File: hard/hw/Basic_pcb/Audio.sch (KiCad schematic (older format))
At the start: 0 parts

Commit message: Bloque de Audio
Bloque de Audio implementado PAM8302 de adafruit:
https://www.adafruit.com/product/2130
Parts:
- added C1: 10uF, Capacitors_SMD:C_0805, symbol C
- added C2, C3: 1uF, Capacitors_SMD:C_0805, symbol C
- added C4, C5: 220pF, Capacitors_SMD:C_0805, symbol C
- added L1, L2: Ferrite_Bead, Resistors_SMD:R_0805, symbol Ferrite_Bead
- added P1: CONN_01X05, Socket_Strips:Socket_Strip_Straight_1x05_Pitch2.54mm, symbol CONN_01X05
- added P2: CONN_01X02, Socket_Strips:Socket_Strip_Straight_1x02_Pitch2.54mm, symbol CONN_01X02
- added R1: 10K, Resistors_SMD:R_0805, symbol R
- added R2, R3: 100, Resistors_SMD:R_0805, symbol R
- added RV1: 10K POT_TRIM, Potentiometers:Potentiometer_Trimmer-EVM3E, symbol POT_TRIM
- added U1: PAM8302A, Housings_SSOP:MSOP-8_3x3mm_Pitch0.65mm, symbol PAM8302A
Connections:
- net labels added: +5V, AIN+, AIN-, GND, ~SD
- wire segments 0 -> 36

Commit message: Actualizacion Power
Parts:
- removed P1: CONN_01X05, Socket_Strips:Socket_Strip_Straight_1x05_Pitch2.54mm, symbol CONN_01X05
- added P?: CONN_01X05, symbol CONN_01X05
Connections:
- net labels added: VCC
- wire segments 36 -> 39
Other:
- moved on the sheet: C1, R1
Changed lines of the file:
@@
 LIBS:rj45_stamp
 LIBS:HDMIspartan6_Board-cache
-LIBS:pam8302-cache
 EELAYER 25 0
 EELAYER END
 $Descr A4 11693 8268
 encoding utf-8
-Sheet 4 5
+Sheet 3 5
 Title ""
 Date ""
@@
 L C C1
 U 1 1 5898CF7F
-P 4650 5400
-F 0 "C1" H 4500 5500 50  0000 L CNN
-F 1 "10uF" H 4450 5300 50  0000 L CNN
-F 2 "Capacitors_SMD:C_0805" H 5200 5400 50  0001 C CNN
-F 3 "" H 4650 5400 50  0000 C CNN
-	1    4650 5400
-	-1   0    0    1
+P 3050 5100
+F 0 "C1" H 2950 5200 50  0000 L CNN
+F 1 "10uF" H 2850 5000 50  0000 L CNN
+F 2 "Capacitors_SMD:C_0805" H 3600 5100 50  0001 C CNN
+F 3 "" H 3050 5100 50  0000 C CNN
+	1    3050 5100
+	-1   0    0    -1
 $EndComp
 $Comp
 L R R1
 U 1 1 5898CF80
-P 5050 5200
-F 0 "R1" V 5130 5200 50  0000 C CNN
-F 1 "10K" V 5050 5200 50  0000 C CNN
-F 2 "Resistors_SMD:R_0805" V 4950 5000 50  0001 C CNN
-F 3 "" H 5050 5200 50  0000 C CNN
-	1    5050 5200
-	0    -1   -1   0
+P 3300 4900
+F 0 "R1" V 3380 4900 50  0000 C CNN
+F 1 "10K" V 3300 4900 50  0000 C CNN
+F 2 "Resistors_SMD:R_0805" V 3200 4700 50  0001 C CNN
+F 3 "" H 3300 4900 50  0000 C CNN
+	1    3300 4900
+	0    1    -1   0
 $EndComp
 $Comp
@@
 $EndComp
 $Comp
-L GND #PWR070
-U 1 1 5898CF83
-P 4650 5700
-F 0 "#PWR070" H 4650 5450 50  0001 C CNN
-F 1 "GND" H 4650 5550 50  0000 C CNN
-F 2 "" H 4650 5700 50  0000 C CNN
-F 3 "" H 4650 5700 50  0000 C CNN
-	1    4650 5700
-	1    0    0    -1
-$EndComp
-$Comp
 L PAM8302A U1
 U 1 1 5898CF84
@@
 $EndComp
 $Comp
-L CONN_01X05 P1
-U 1 1 5898CF85
-P 2700 3700
-F 0 "P1" H 2700 4000 50  0000 C CNN
-F 1 "CONN_01X05" V 2800 3700 50  0000 C CNN
-F 2 "Socket_Strips:Socket_Strip_Straight_1x05_Pitch2.54mm" H 2700 3700 50  0001 C CNN
-F 3 "" H 2700 3700 50  0000 C CNN
-	1    2700 3700
-	-1   0    0    1
-$EndComp
-$Comp
 L CONN_01X02 P2
 U 1 1 5898CF86
@@
 ~SD
 $Comp
-L GND #PWR071
+L GND #PWR060
 U 1 1 5898CF87
 P 3250 3900
-F 0 "#PWR071" H 3250 3650 50  0001 C CNN
+F 0 "#PWR060" H 3250 3650 50  0001 C CNN
 F 1 "GND" H 3250 3750 50  0000 C CNN
 F 2 "" H 3250 3900 50  0000 C CNN
@@
 $EndComp
 $Comp
-L +5V #PWR072
+L +5V #PWR061
 U 1 1 5898CF88
 P 3250 3750
-F 0 "#PWR072" H 3250 3600 50  0001 C CNN
+F 0 "#PWR061" H 3250 3600 50  0001 C CNN
 F 1 "+5V" H 3250 3890 50  0000 C CNN
 F 2 "" H 3250 3750 50  0000 C CNN
@@
 $EndComp
 $Comp
-L GND #PWR073
+L GND #PWR062
 U 1 1 5898CF89
 P 7300 3600
-F 0 "#PWR073" H 7300 3350 50  0001 C CNN
+F 0 "#PWR062" H 7300 3350 50  0001 C CNN
 F 1 "GND" H 7300 3450 50  0000 C CNN
 F 2 "" H 7300 3600 50  0000 C CNN
@@
 $EndComp
 $Comp
-L +5V #PWR074
+L +5V #PWR063
 U 1 1 5898CF8A
 P 7150 3700
-F 0 "#PWR074" H 7150 3550 50  0001 C CNN
+F 0 "#PWR063" H 7150 3550 50  0001 C CNN
 F 1 "+5V" H 7150 3840 50  0000 C CNN
 F 2 "" H 7150 3700 50  0000 C CNN
@@
 $EndComp
 $Comp
-L GND #PWR075
+L GND #PWR064
 U 1 1 5898CF90
 P 8200 3700
-F 0 "#PWR075" H 8200 3450 50  0001 C CNN
+F 0 "#PWR064" H 8200 3450 50  0001 C CNN
 F 1 "GND" H 8200 3550 50  0000 C CNN
 F 2 "" H 8200 3700 50  0000 C CNN
@@
 $EndComp
 $Comp
-L GND #PWR076
+L GND #PWR065
 U 1 1 5898CF92
 P 8200 4500
-F 0 "#PWR076" H 8200 4250 50  0001 C CNN
+F 0 "#PWR065" H 8200 4250 50  0001 C CNN
 F 1 "GND" H 8200 4350 50  0000 C CNN
 F 2 "" H 8200 4500 50  0000 C CNN
@@
 Text Label 5950 3500 0    60   ~ 0
 ~SD
+Text Label 3750 4500 2    60   ~ 0
+~SD
+Text HLabel 2850 4900 0    60   Input ~ 0
+VCC
+Text HLabel 2850 5300 0    60   Input ~ 0
+GND
+$Comp
+L +5V #PWR?
+U 1 1 589F6407
+P 3050 4800
+F 0 "#PWR?" H 3050 4650 50  0001 C CNN
+F 1 "+5V" H 3050 4940 50  0000 C CNN
+F 2 "" H 3050 4800 50  0000 C CNN
+F 3 "" H 3050 4800 50  0000 C CNN
+	1    3050 4800
+	1    0    0    -1
+$EndComp
+$Comp
+L GND #PWR?
+U 1 1 589F6490
+P 3050 5400
+F 0 "#PWR?" H 3050 5150 50  0001 C CNN
+F 1 "GND" H 3050 5250 50  0000 C CNN
+F 2 "" H 3050 5400 50  0000 C CNN
+F 3 "" H 3050 5400 50  0000 C CNN
+	1    3050 5400
+	1    0    0    -1
+$EndComp
+Text HLabel 2850 4500 0    60   Input ~ 0
+~SD
 Wire Wire Line
 	6100 3500 5850 3500
@@
 Wire Wire Line
 	3100 3500 2900 3500
-$Comp
-L +5V #PWR077
-U 1 1 5898CF93
-P 4650 5100
-F 0 "#PWR077" H 4650 4950 50  0001 C CNN
-F 1 "+5V" H 4650 5240 50  0000 C CNN
-F 2 "" H 4650 5100 50  0000 C CNN
-F 3 "" H 4650 5100 50  0000 C CNN
-	1    4650 5100
-	1    0    0    -1
-$EndComp
-Wire Wire Line
-	5200 5200 5500 5200
-Text Label 5350 5200 0    60   ~ 0
-~SD
 Wire Wire Line
 	3250 3800 3250 3750
 Connection ~ 4650 4150
 Wire Wire Line
-	8600 3250 7800 3250
-Wire Wire Line
-	8600 4000 7800 4000
+	7800 3250 8600 3250
+Wire Wire Line
+	7800 4000 8600 4000
 Wire Wire Line
 	5500 3700 5300 3700
@@
 	5500 4150 5300 4150
 Wire Wire Line
-	4650 5100 4650 5250
-Wire Wire Line
-	4900 5200 4650 5200
-Connection ~ 4650 5200
-Wire Wire Line
-	4650 5550 4650 5700
+	3050 4800 3050 4950
+Wire Wire Line
+	3050 5250 3050 5400
+Connection ~ 3050 4900
+Connection ~ 3050 5300
+$Comp
+L CONN_01X05 P?
+U 1 1 58A0B165
+P 2700 3700
+F 0 "P?" H 2700 4000 50  0000 C CNN
+F 1 "CONN_01X05" V 2800 3700 50  0000 C CNN
+F 2 "" H 2700 3700 50  0000 C CNN
+F 3 "" H 2700 3700 50  0000 C CNN
+	1    2700 3700
+	-1   0    0    1
+$EndComp
+Wire Wire Line
+	2850 5300 3050 5300
+Wire Wire Line
+	3550 4900 3550 4500
+Connection ~ 3550 4500
+Wire Wire Line
+	3450 4900 3550 4900
+Wire Wire Line
+	3150 4900 2850 4900
+Wire Wire Line
+	3800 4500 2850 4500
 $EndSCHEMATC

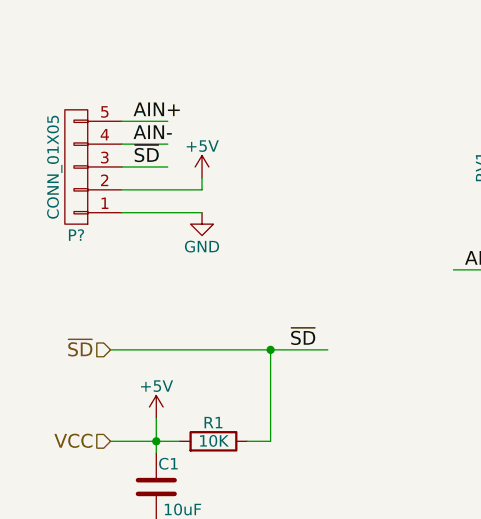
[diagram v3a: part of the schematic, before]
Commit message: Fuente 12V
by Luis Yaya
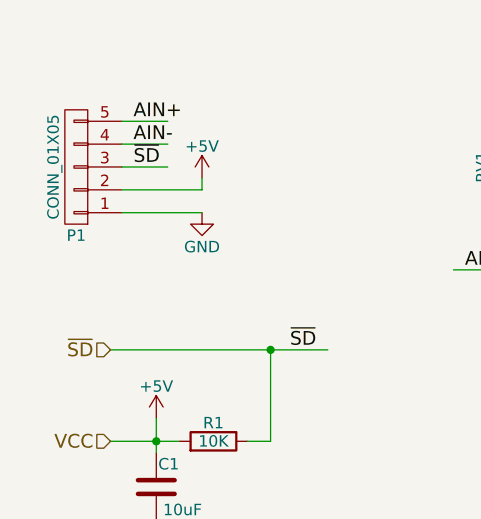
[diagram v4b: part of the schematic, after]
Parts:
- gave numbers to parts that had none: 1
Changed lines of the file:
@@
 LIBS:rj45_stamp
 LIBS:HDMIspartan6_Board-cache
-LIBS:fuente-cache
 EELAYER 25 0
 EELAYER END
@@
 ~SD
 $Comp
-L GND #PWR060
+L GND #PWR026
 U 1 1 5898CF87
 P 3250 3900
-F 0 "#PWR060" H 3250 3650 50  0001 C CNN
+F 0 "#PWR026" H 3250 3650 50  0001 C CNN
 F 1 "GND" H 3250 3750 50  0000 C CNN
 F 2 "" H 3250 3900 50  0000 C CNN
@@
 $EndComp
 $Comp
-L +5V #PWR061
+L +5V #PWR027
 U 1 1 5898CF88
 P 3250 3750
-F 0 "#PWR061" H 3250 3600 50  0001 C CNN
+F 0 "#PWR027" H 3250 3600 50  0001 C CNN
 F 1 "+5V" H 3250 3890 50  0000 C CNN
 F 2 "" H 3250 3750 50  0000 C CNN
@@
 $EndComp
 $Comp
-L GND #PWR062
+L GND #PWR028
 U 1 1 5898CF89
 P 7300 3600
-F 0 "#PWR062" H 7300 3350 50  0001 C CNN
+F 0 "#PWR028" H 7300 3350 50  0001 C CNN
 F 1 "GND" H 7300 3450 50  0000 C CNN
 F 2 "" H 7300 3600 50  0000 C CNN
@@
 $EndComp
 $Comp
-L +5V #PWR063
+L +5V #PWR029
 U 1 1 5898CF8A
 P 7150 3700
-F 0 "#PWR063" H 7150 3550 50  0001 C CNN
+F 0 "#PWR029" H 7150 3550 50  0001 C CNN
 F 1 "+5V" H 7150 3840 50  0000 C CNN
 F 2 "" H 7150 3700 50  0000 C CNN
@@
 $EndComp
 $Comp
-L GND #PWR064
+L GND #PWR030
 U 1 1 5898CF90
 P 8200 3700
-F 0 "#PWR064" H 8200 3450 50  0001 C CNN
+F 0 "#PWR030" H 8200 3450 50  0001 C CNN
 F 1 "GND" H 8200 3550 50  0000 C CNN
 F 2 "" H 8200 3700 50  0000 C CNN
@@
 $EndComp
 $Comp
-L GND #PWR065
+L GND #PWR031
 U 1 1 5898CF92
 P 8200 4500
-F 0 "#PWR065" H 8200 4250 50  0001 C CNN
+F 0 "#PWR031" H 8200 4250 50  0001 C CNN
 F 1 "GND" H 8200 4350 50  0000 C CNN
 F 2 "" H 8200 4500 50  0000 C CNN
@@
 GND
 $Comp
-L +5V #PWR?
+L +5V #PWR032
 U 1 1 589F6407
 P 3050 4800
-F 0 "#PWR?" H 3050 4650 50  0001 C CNN
+F 0 "#PWR032" H 3050 4650 50  0001 C CNN
 F 1 "+5V" H 3050 4940 50  0000 C CNN
 F 2 "" H 3050 4800 50  0000 C CNN
@@
 $EndComp
 $Comp
-L GND #PWR?
+L GND #PWR033
 U 1 1 589F6490
 P 3050 5400
-F 0 "#PWR?" H 3050 5150 50  0001 C CNN
+F 0 "#PWR033" H 3050 5150 50  0001 C CNN
 F 1 "GND" H 3050 5250 50  0000 C CNN
 F 2 "" H 3050 5400 50  0000 C CNN
@@
 Connection ~ 3050 5300
 $Comp
-L CONN_01X05 P?
+L CONN_01X05 P1
 U 1 1 58A0B165
 P 2700 3700
-F 0 "P?" H 2700 4000 50  0000 C CNN
+F 0 "P1" H 2700 4000 50  0000 C CNN
 F 1 "CONN_01X05" V 2800 3700 50  0000 C CNN
-F 2 "" H 2700 3700 50  0000 C CNN
+F 2 "" H 2700 3700 50  0001 C CNN
 F 3 "" H 2700 3700 50  0000 C CNN
 	1    2700 3700

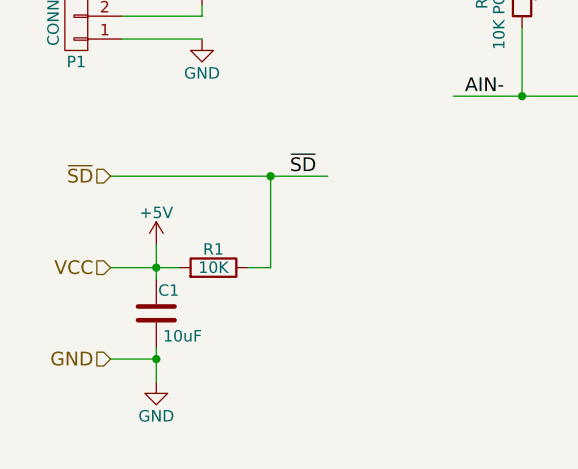
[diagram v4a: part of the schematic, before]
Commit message: Actualización PinOut LVDS
by Rubén Parra
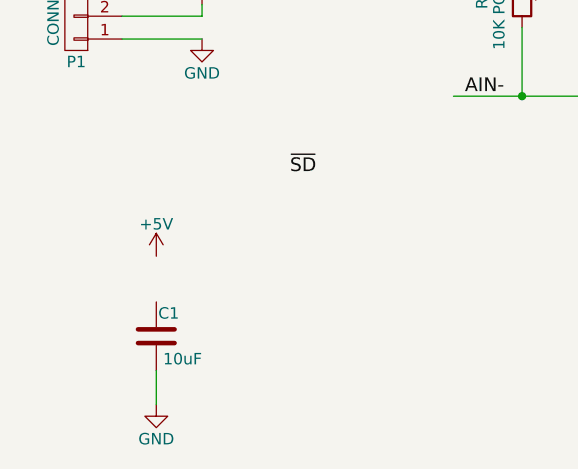
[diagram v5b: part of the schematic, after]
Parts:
- removed R1: 10K, Resistors_SMD:R_0805, symbol R
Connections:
- net labels removed: VCC
- wire segments 39 -> 33
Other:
- moved on the sheet: C1
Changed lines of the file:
@@
 L C C1
 U 1 1 5898CF7F
-P 3050 5100
-F 0 "C1" H 2950 5200 50  0000 L CNN
-F 1 "10uF" H 2850 5000 50  0000 L CNN
-F 2 "Capacitors_SMD:C_0805" H 3600 5100 50  0001 C CNN
-F 3 "" H 3050 5100 50  0000 C CNN
-	1    3050 5100
+P 3050 5200
+F 0 "C1" H 2950 5300 50  0000 L CNN
+F 1 "10uF" H 2850 5100 50  0000 L CNN
+F 2 "Capacitors_SMD:C_0805" H 3600 5200 50  0001 C CNN
+F 3 "" H 3050 5200 50  0000 C CNN
+	1    3050 5200
 	-1   0    0    -1
-$EndComp
-$Comp
-L R R1
-U 1 1 5898CF80
-P 3300 4900
-F 0 "R1" V 3380 4900 50  0000 C CNN
-F 1 "10K" V 3300 4900 50  0000 C CNN
-F 2 "Resistors_SMD:R_0805" V 3200 4700 50  0001 C CNN
-F 3 "" H 3300 4900 50  0000 C CNN
-	1    3300 4900
-	0    1    -1   0
 $EndComp
 $Comp
@@
 Text Label 3750 4500 2    60   ~ 0
 ~SD
-Text HLabel 2850 4900 0    60   Input ~ 0
-VCC
-Text HLabel 2850 5300 0    60   Input ~ 0
-GND
 $Comp
 L +5V #PWR032
 U 1 1 589F6407
-P 3050 4800
-F 0 "#PWR032" H 3050 4650 50  0001 C CNN
-F 1 "+5V" H 3050 4940 50  0000 C CNN
-F 2 "" H 3050 4800 50  0000 C CNN
-F 3 "" H 3050 4800 50  0000 C CNN
-	1    3050 4800
+P 3050 4850
+F 0 "#PWR032" H 3050 4700 50  0001 C CNN
+F 1 "+5V" H 3050 4990 50  0000 C CNN
+F 2 "" H 3050 4850 50  0000 C CNN
+F 3 "" H 3050 4850 50  0000 C CNN
+	1    3050 4850
 	1    0    0    -1
 $EndComp
@@
 L GND #PWR033
 U 1 1 589F6490
-P 3050 5400
-F 0 "#PWR033" H 3050 5150 50  0001 C CNN
-F 1 "GND" H 3050 5250 50  0000 C CNN
-F 2 "" H 3050 5400 50  0000 C CNN
-F 3 "" H 3050 5400 50  0000 C CNN
-	1    3050 5400
-	1    0    0    -1
-$EndComp
-Text HLabel 2850 4500 0    60   Input ~ 0
-~SD
-Wire Wire Line
-	6100 3500 5850 3500
-Wire Wire Line
-	8600 4000 8600 3700
-Wire Wire Line
-	8600 3250 8600 3600
-Connection ~ 8200 3250
-Wire Wire Line
-	8200 4000 8200 4100
-Wire Wire Line
-	8200 3650 8200 3700
-Wire Wire Line
-	8200 3350 8200 3250
-Wire Wire Line
-	8200 4400 8200 4500
-Connection ~ 8200 4000
-Wire Wire Line
-	7250 3800 7100 3800
-Wire Wire Line
-	7250 4000 7250 3800
-Wire Wire Line
-	7500 4000 7250 4000
-Wire Wire Line
-	7250 3500 7100 3500
-Wire Wire Line
-	7250 3250 7250 3500
-Wire Wire Line
-	7500 3250 7250 3250
-Wire Wire Line
-	4650 3550 4650 3300
-Wire Wire Line
-	4350 4150 5000 4150
-Wire Wire Line
-	4650 3850 4650 4150
-Wire Wire Line
-	5000 3700 4800 3700
-Wire Wire Line
-	6100 4150 5800 4150
-Wire Wire Line
-	6100 3800 6100 4150
-Wire Wire Line
-	6100 3700 5800 3700
-Wire Wire Line
-	7150 3700 7100 3700
-Wire Wire Line
-	7300 3600 7100 3600
-Wire Wire Line
-	2900 3900 3250 3900
-Wire Wire Line
-	2900 3800 3250 3800
-Wire Wire Line
-	3100 3700 2900 3700
-Wire Wire Line
-	3100 3600 2900 3600
-Wire Wire Line
-	3100 3500 2900 3500
-Wire Wire Line
-	3250 3800 3250 3750
-Connection ~ 4650 4150
-Wire Wire Line
-	7800 3250 8600 3250
-Wire Wire Line
-	7800 4000 8600 4000
-Wire Wire Line
-	5500 3700 5300 3700
-Wire Wire Line
-	5500 4150 5300 4150
-Wire Wire Line
-	3050 4800 3050 4950
-Wire Wire Line
-	3050 5250 3050 5400
-Connection ~ 3050 4900
-Connection ~ 3050 5300
+P 3050 5500
+F 0 "#PWR033" H 3050 5250 50  0001 C CNN
+F 1 "GND" H 3050 5350 50  0000 C CNN
+F 2 "" H 3050 5500 50  0000 C CNN
+F 3 "" H 3050 5500 50  0000 C CNN
+	1    3050 5500
+	1    0    0    -1
+$EndComp
 $Comp
 L CONN_01X05 P1
@@
 $EndComp
 Wire Wire Line
-	2850 5300 3050 5300
-Wire Wire Line
-	3550 4900 3550 4500
-Connection ~ 3550 4500
-Wire Wire Line
-	3450 4900 3550 4900
-Wire Wire Line
-	3150 4900 2850 4900
-Wire Wire Line
-	3800 4500 2850 4500
+	3050 5350 3050 5500
+Wire Wire Line
+	5500 4150 5300 4150
+Wire Wire Line
+	5500 3700 5300 3700
+Wire Wire Line
+	7800 4000 8600 4000
+Wire Wire Line
+	7800 3250 8600 3250
+Connection ~ 4650 4150
+Wire Wire Line
+	3250 3800 3250 3750
+Wire Wire Line
+	3100 3500 2900 3500
+Wire Wire Line
+	3100 3600 2900 3600
+Wire Wire Line
+	3100 3700 2900 3700
+Wire Wire Line
+	2900 3800 3250 3800
+Wire Wire Line
+	2900 3900 3250 3900
+Wire Wire Line
+	7300 3600 7100 3600
+Wire Wire Line
+	7150 3700 7100 3700
+Wire Wire Line
+	6100 3700 5800 3700
+Wire Wire Line
+	6100 3800 6100 4150
+Wire Wire Line
+	6100 4150 5800 4150
+Wire Wire Line
+	5000 3700 4800 3700
+Wire Wire Line
+	4650 3850 4650 4150
+Wire Wire Line
+	4350 4150 5000 4150
+Wire Wire Line
+	4650 3550 4650 3300
+Wire Wire Line
+	7500 3250 7250 3250
+Wire Wire Line
+	7250 3250 7250 3500
+Wire Wire Line
+	7250 3500 7100 3500
+Wire Wire Line
+	7500 4000 7250 4000
+Wire Wire Line
+	7250 4000 7250 3800
+Wire Wire Line
+	7250 3800 7100 3800
+Connection ~ 8200 4000
+Wire Wire Line
+	8200 4400 8200 4500
+Wire Wire Line
+	8200 3350 8200 3250
+Wire Wire Line
+	8200 3650 8200 3700
+Wire Wire Line
+	8200 4000 8200 4100
+Connection ~ 8200 3250
+Wire Wire Line
+	8600 3250 8600 3600
+Wire Wire Line
+	8600 4000 8600 3700
+Wire Wire Line
+	6100 3500 5850 3500
 $EndSCHEMATC

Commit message: Actualizacion Raiz
por Rubén
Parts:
- added R1: 10k, Resistors_SMD:R_0805, symbol R
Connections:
- wire segments 33 -> 36
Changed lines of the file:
@@
 Text Label 5950 3500 0    60   ~ 0
 ~SD
-Text Label 3750 4500 2    60   ~ 0
+Text Label 3800 4950 2    60   ~ 0
 ~SD
 $Comp
@@
 Wire Wire Line
 	6100 3500 5850 3500
+Wire Wire Line
+	3050 4850 3050 5050
+$Comp
+L R R1
+U 1 1 589D33B2
+P 3450 4950
+F 0 "R1" V 3530 4950 50  0000 C CNN
+F 1 "10k" V 3450 4950 50  0000 C CNN
+F 2 "Resistors_SMD:R_0805" V 3380 4950 50  0001 C CNN
+F 3 "" H 3450 4950 50  0000 C CNN
+	1    3450 4950
+	0    1    1    0
+$EndComp
+Wire Wire Line
+	2750 4950 3300 4950
+Connection ~ 3050 4950
+Wire Wire Line
+	3850 4950 3600 4950
+Text HLabel 2750 4950 0    60   Input ~ 0
+~SD
 $EndSCHEMATC
